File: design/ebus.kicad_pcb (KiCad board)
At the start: 2 copper layers, 84.3 x 56.9 mm, 51 parts, among them J1 EBUS, J10 Measurements, J2 UART, J3 USB_B_Micro, J4 PWR, J5 SERVICE, J6 PROG, J7 TX test, J8 TX switch, J9 RX switch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

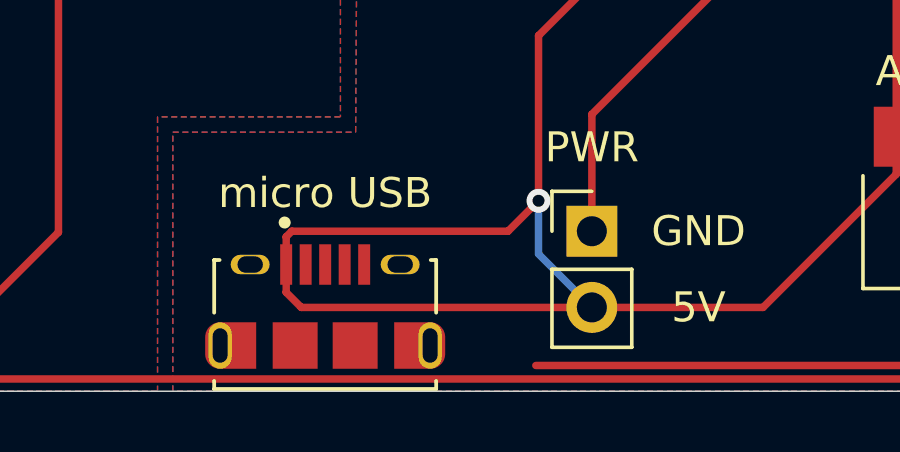
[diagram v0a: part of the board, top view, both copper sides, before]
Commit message: Fix missing track
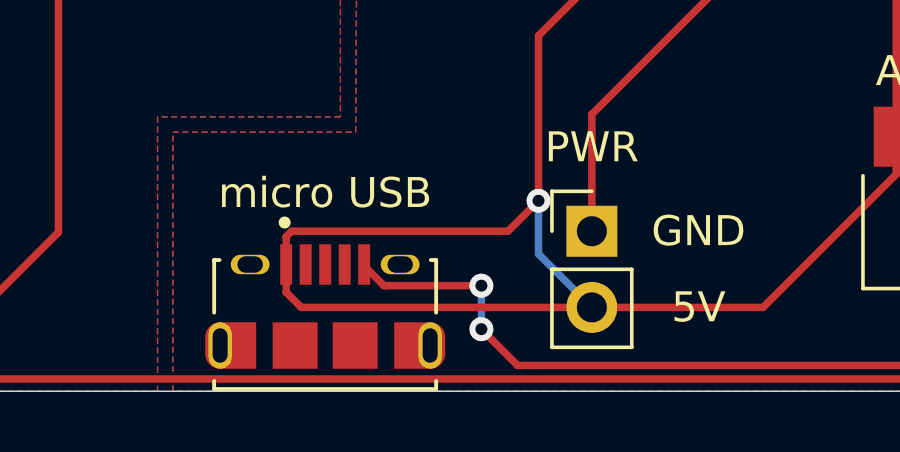
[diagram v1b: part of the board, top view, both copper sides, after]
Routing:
- net GNDREF: track 185.7 -> 193.7 mm, vias 4 -> 6
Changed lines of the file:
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@@
     (thickness 1.6)
     (drawings 82)
-    (tracks 436)
+    (tracks 444)
     (zones 0)
     (modules 51)
@@
   (segment (start 85.09 118.695) (end 83.090001 116.695001) (width 0.25) (layer B.Cu) (net 1))
   (segment (start 85.09 121.412) (end 85.09 118.695) (width 0.25) (layer B.Cu) (net 1))
+  (via (at 96.647 137.631) (size 0.8) (drill 0.4) (layers F.Cu B.Cu) (net 1))
+  (segment (start 97.857001 138.841001) (end 96.647 137.631) (width 0.25) (layer F.Cu) (net 1))
+  (segment (start 98.462001 138.841001) (end 97.857001 138.841001) (width 0.25) (layer F.Cu) (net 1))
+  (via (at 96.647 136.181) (size 0.8) (drill 0.4) (layers F.Cu B.Cu) (net 1))
+  (segment (start 96.647 137.631) (end 96.647 136.181) (width 0.25) (layer B.Cu) (net 1))
+  (segment (start 92.74 135.520252) (end 92.74 135.476) (width 0.25) (layer F.Cu) (net 1))
+  (segment (start 93.400748 136.181) (end 92.74 135.520252) (width 0.25) (layer F.Cu) (net 1))
+  (segment (start 96.647 136.181) (end 93.400748 136.181) (width 0.25) (layer F.Cu) (net 1))
   (segment (start 110.476 132.466) (end 110.476 131.216) (width 0.25) (layer F.Cu) (net 2))
   (segment (start 106.036 136.906) (end 110.476 132.466) (width 0.25) (layer F.Cu) (net 2))
